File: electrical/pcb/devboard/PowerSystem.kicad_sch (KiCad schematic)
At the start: 23 parts, among them J1 Barrel_Jack, Q1 NMOS, Q2 NMOS, U1 LM51561HPWP

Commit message: minor stuff
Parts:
- added U3: AMS1117-3.3, Package_TO_SOT_SMD:SOT-223-3_TabPin2, symbol Regulator_Linear:AMS1117-3.3
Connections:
- net +215V renamed SUPPLY
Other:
- note added: "+22 <-> +26 VIN"
- note added: "IOut = 0.5A or 625 Braille Cells but 120W!!!"
- note added: "OPTIONAL: CURRENT SENSE"
- note added: "TODO: SUPPLY to 3.3V for ESP32"
- note added: "TODO: TEMP SENSOR"
- note added: "TODO: USBV to 3.3V for ESP32"
- note removed: "IOut = 0.5A or 625 Braille Cells"
- title: (none) -> Power System HV DC/DC
- moved on the sheet: R1

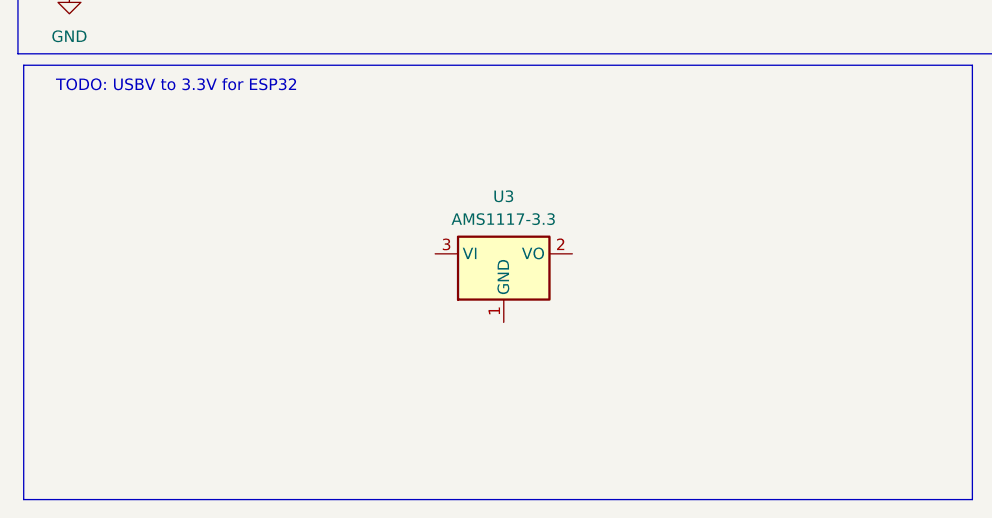
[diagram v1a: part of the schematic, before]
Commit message: cell shifter routed
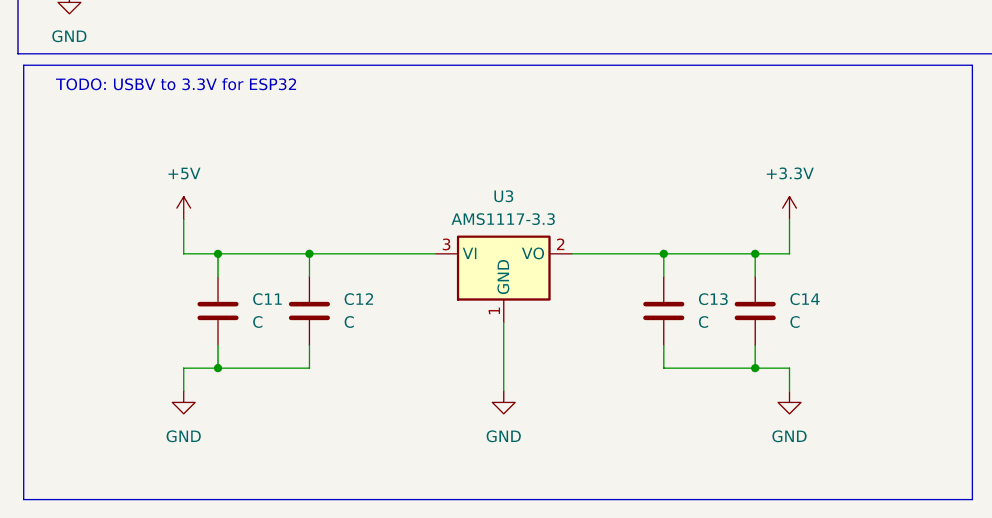
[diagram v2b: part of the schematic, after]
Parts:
- added C11, C12, C13, C14: C, symbol Device:C
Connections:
- net GND: now also U3.1 (GND), C11.2, C12.2, C13.2, C14.2
- net +3.3V: now reaches U3.2 (VO)
- net +3.3V: now also C13.1, C14.1
- net +5V: now reaches U3.3 (VI)
- net +5V: now also C11.1, C12.1

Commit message: Add files via upload
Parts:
- removed C1: 4.7uF, symbol Device:C_Polarized_US
- removed C4: 1uF, symbol Device:C
- removed C5: 1nF, symbol Device:C
- removed C6: 470nF, symbol Device:C
- removed C8: 4uF, symbol Device:C
- removed L1: 33uH, symbol Device:L
- removed R7: 2k49, symbol Device:R
- removed U1: LM51561HPWP, Package_SO:Texas_HTSSOP-14-1EP_4.4x5mm_P0.65mm_EP3.4x5mm_Mask3.155x3.255mm_ThermalVias, symbol Regulator_Switching:LM51561HPWP
- added C1: 4uF, Capacitor_SMD:C_0603_1608Metric, symbol Device:C
- added C17: 10uF, Capacitor_SMD:C_0603_1608Metric, symbol Device:C
- added C18, C20: 0.1uF, Capacitor_SMD:C_0603_1608Metric, symbol Device:C
- added C19: 22uF, Capacitor_SMD:C_0603_1608Metric, symbol Device:C
- added Chf1: 120pF, Capacitor_SMD:C_0603_1608Metric, symbol Device:C
- added Css1: 100nF, Capacitor_SMD:C_0603_1608Metric, symbol Device:C
- added L2: 2.2uH, Inductor_SMD:L_6.3x6.3_H3, symbol Device:L
- added NT1: NetTie_2, NetTie:NetTie-2_SMD_Pad0.5mm, symbol Device:NetTie_2
- added R12: 10k, Resistor_SMD:R_0603_1608Metric, symbol Device:R
- added R13: R_Shunt, Resistor_SMD:R_0603_1608Metric, symbol Device:R_Shunt
- added Rcs1: 0.1Ω, Resistor_SMD:R_0603_1608Metric, symbol Device:R
- added Rtop1: 200kΩ, Resistor_SMD:R_0603_1608Metric, symbol Device:R
- added T1: Transformer_1P_1S, Resistor_SMD:R_0603_1608Metric_Pad0.98x0.95mm_HandSolder, symbol Device:Transformer_1P_1S
- added TH1: Thermistor_NTC, Resistor_SMD:R_0603_1608Metric_Pad0.98x0.95mm_HandSolder, symbol Device:Thermistor_NTC
- added U4: TPS62162DSG, Package_SON:WSON-8-1EP_2x2mm_P0.5mm_EP0.9x1.6mm_ThermalVias, symbol Regulator_Switching:TPS62162DSG
- added U5: INA219AxD, Package_SO:SOIC-8_3.9x4.9mm_P1.27mm, symbol Sensor_Energy:INA219AxD
- added U6: LM5185QPWPRQ1, Package_SO:Texas_HTSSOP-14-1EP_4.4x5mm_P0.65mm_EP3.4x5mm_Mask3.155x3.255mm_ThermalVias, symbol 2026-02-07_14-23-52:LM5185QPWPRQ1
- C11, C12, C13, C14: footprint (none) -> Capacitor_SMD:C_0603_1608Metric
- C2: value 100nF -> 1.2uF; footprint (none) -> Capacitor_SMD:C_0603_1608Metric
- C3: value 56nF -> 47pF; footprint (none) -> Capacitor_SMD:C_0603_1608Metric
- C7: value 100nF -> CIN; footprint (none) -> Capacitor_SMD:C_0603_1608Metric
- Cvcc1: renamed from C9; value 1.2uF -> 1uF; footprint (none) -> Capacitor_SMD:C_0603_1608Metric
- D1: footprint (none) -> Diode_SMD:D_SOD-123
- D2: footprint (none) -> Diode_SMD:D_SMA
- J1: footprint (none) -> Connector_BarrelJack:BarrelJack_CUI_PJ-102AH_Horizontal
- Q1, Q2: footprint (none) -> Package_SO:SO-8_3.9x4.9mm_P1.27mm
- R1: footprint (none) -> Resistor_SMD:R_0603_1608Metric
- R2: value 48k7 -> 100Ω; footprint (none) -> Resistor_SMD:R_0603_1608Metric
- R3: value 1k -> 360kΩ; footprint (none) -> Resistor_SMD:R_0603_1608Metric
- R4: value 100 -> 10kΩ; footprint (none) -> Resistor_SMD:R_0603_1608Metric
- R5: value 2k67 -> RCOMP; footprint (none) -> Resistor_SMD:R_0603_1608Metric
- R6: value 532k86 -> RCOMP; footprint (none) -> Resistor_SMD:R_0603_1608Metric
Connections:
- net +24V: now also C3.2, C7.1, R4.1, R5.2, R6.2, Chf1.2, Css1.2, NT1.2, R13.1, R13.2, R13.3, R13.4, Rtop1.1, T1.1 (AA), U5.7 (IN-), U5.8 (IN+), U6.14 (VIN), U6.15 (EP), U6.5 (AGND); no longer C2.1
- net +5V: now also C17.1, C18.2, U4.3 (EN)
- net GND: now also C1.2, C17.2, C19.1, C19.2, C20.1, C20.2, L2.2, T1.4 (SB), TH1.1, U4.4 (AGND), U4.5 (FB), U4.6 (VOS), U5.1 (A1), U5.2 (A0), U5.6 (GND); no longer C3.2, Cvcc1.2, R2.2, R5.1
- net SUPPLY: no longer Cvcc1.1, D2.1 (K), R6.2
- net GNDPWR: now reaches C7.2
- net GNDPWR: now also Cvcc1.2, NT1.1, Rcs1.1, U6.8 (PGND); no longer R5.2
- net at Q2.1 (D): now also R3.2, T1.2 (AB); no longer D2.2 (A)
- net at C3.1: now also R2.1, U6.9 (CS)
- net at Q2.2 (G): now also U6.11 (GATE)
- net at Q2.3 (S): now also R2.2, Rcs1.2; no longer R4.2
- net COMP: now reaches R6.1
- net COMP: now also R5.1, Chf1.1, U6.7 (COMP)
- net at R3.1: now also U6.13 (FB)
- new net: Cvcc1.1, U6.10 (VCC)
- new net: D2.2 (A), T1.3 (SA)
- new net: Rtop1.2, U6.1 (EN)
- new net: R4.2, U6.4 (RSET)
- new net: Css1.1, U6.6 (SS)
- new net: C18.1, U4.2 (VIN)
- new net: L2.1, U4.7 (SW)
- new net +3V3: R12.1, U5.5 (VS)
- new net +450V: C1.1, C2.1, D2.1 (K)
- new net SCL: U5.4 (SCL)
- new net SDA: U5.3 (SDA)
- new net TEMP_VAL: R12.2, TH1.2
- no-connect marks 1 -> 0
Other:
- moved on the sheet: Cvcc1, D2, Q2
